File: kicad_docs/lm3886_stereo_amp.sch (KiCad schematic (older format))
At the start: 22 parts, among them J1 signal_in, J2 speaker_out, J3 power_in, U1 LM3886

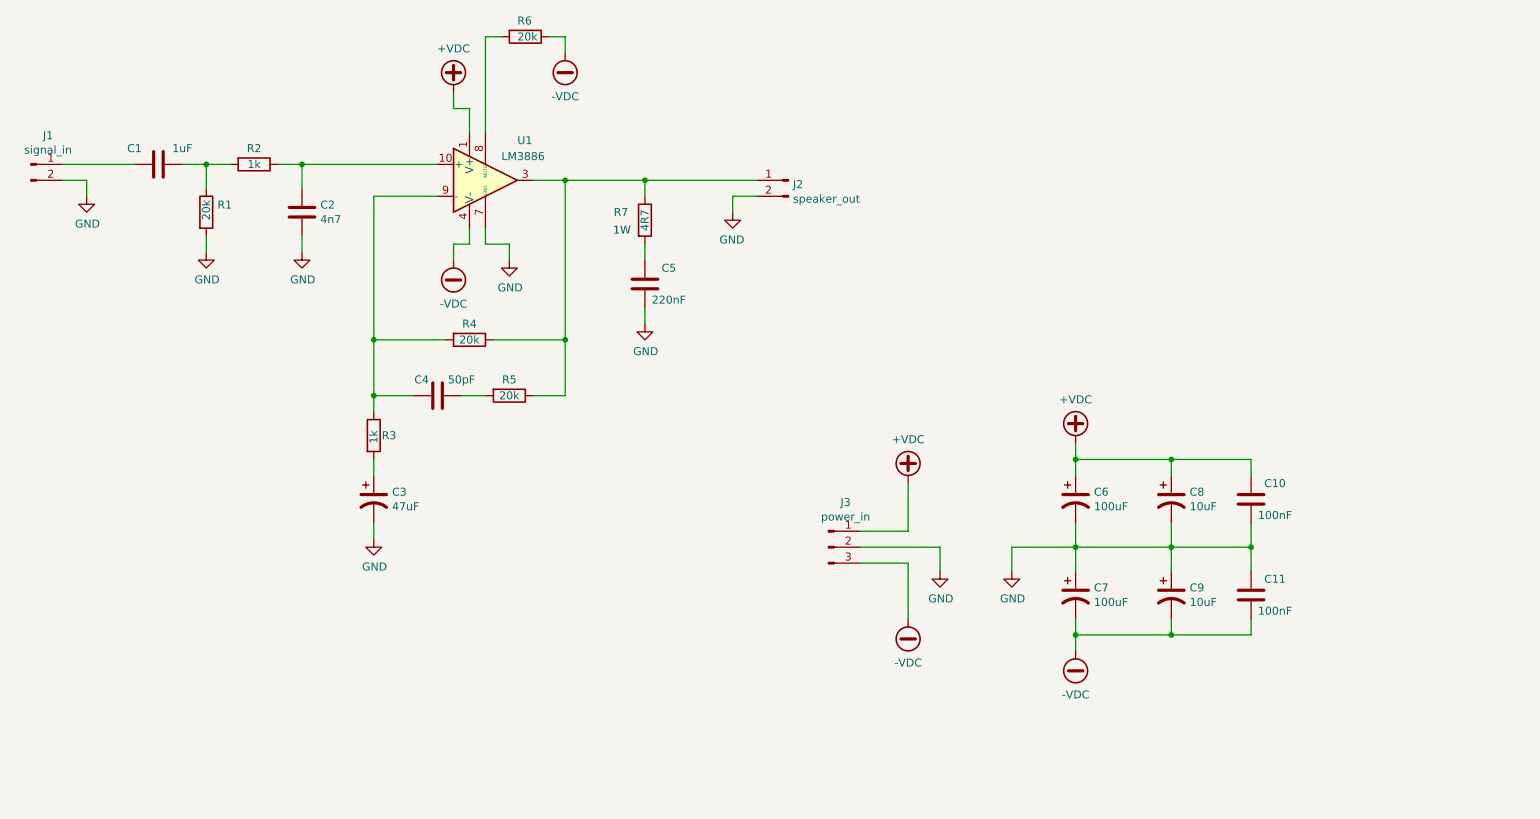
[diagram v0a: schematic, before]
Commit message: redesign pcb for easier to source components
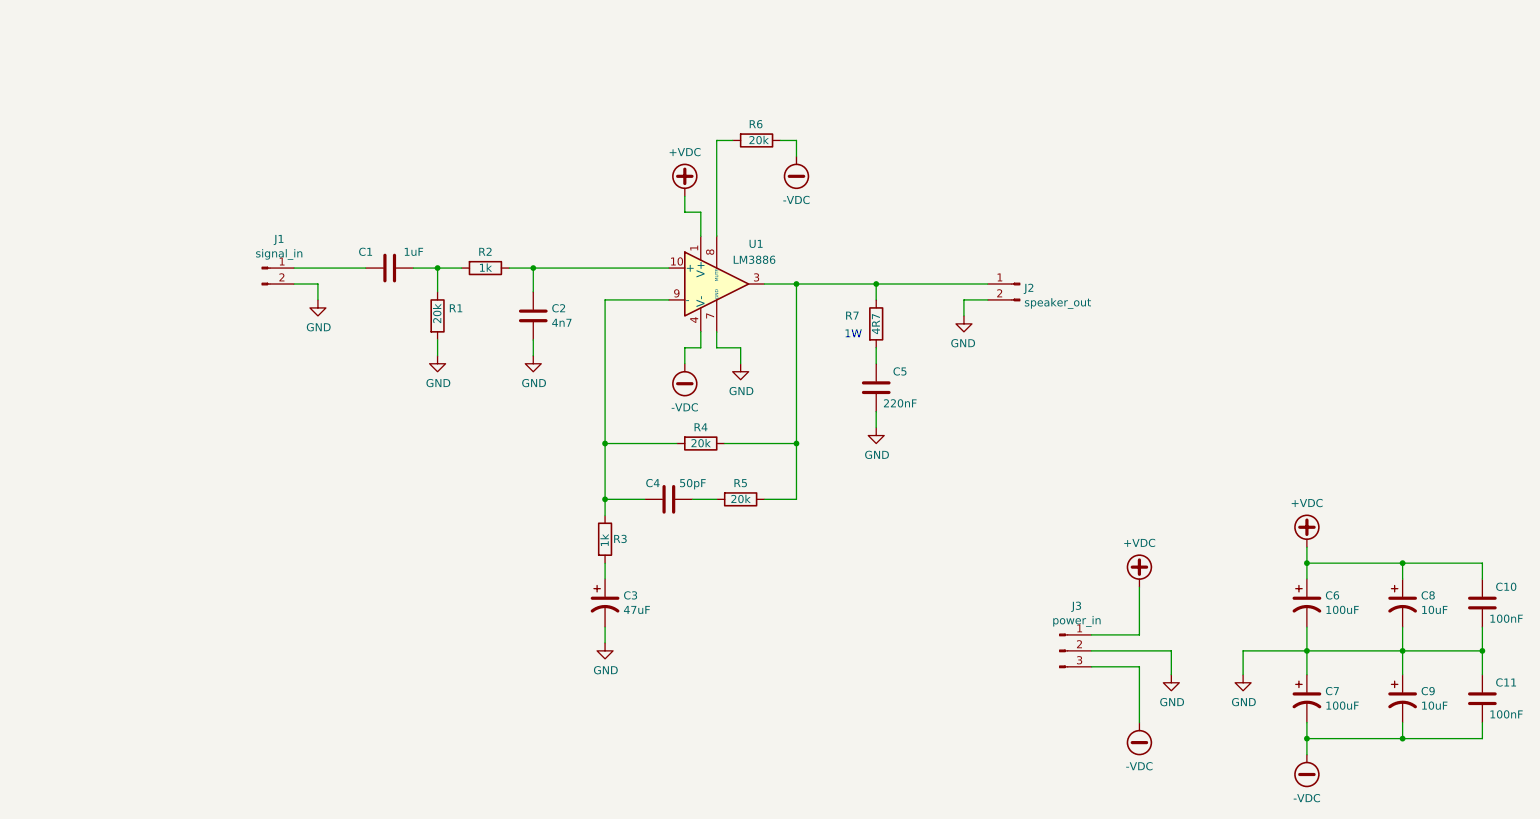
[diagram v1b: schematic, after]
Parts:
- C1, C5: footprint Capacitor_SMD:C_2220_5650Metric_Pad1.97x5.40mm_HandSolder -> Capacitor_THT:C_Rect_L7.0mm_W3.5mm_P5.00mm
- C2: footprint Capacitor_SMD:C_0805_2012Metric_Pad1.15x1.40mm_HandSolder -> Capacitor_THT:C_Rect_L7.0mm_W2.5mm_P5.00mm
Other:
- moved on the sheet: C1, C10, C11, C2, C3, C4, C5, C6, C7, C8, C9, J1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
